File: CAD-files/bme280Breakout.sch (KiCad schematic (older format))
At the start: 9 parts, among them J1 Conn_01x04_Male, U1 BME280

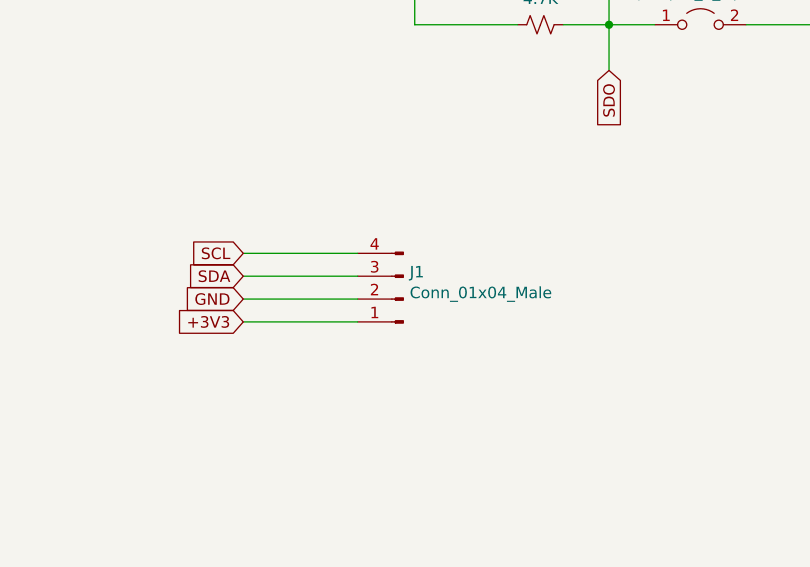
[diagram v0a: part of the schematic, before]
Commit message: added castellated holes
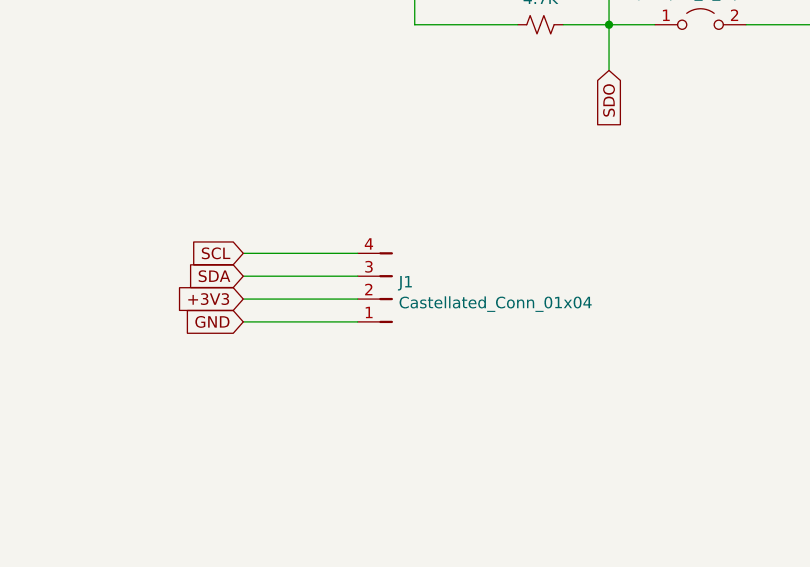
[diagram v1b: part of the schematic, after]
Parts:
- removed J1: Conn_01x04_Male, Connector_PinHeader_2.54mm:PinHeader_1x04_P2.54mm_Vertical, symbol Connector:Conn_01x04_Male
- added J1: Castellated_Conn_01x04, DS-connectors:Castellated_PinHeader_01x04_P2.54mm_Vertical, symbol DS-connectors:Castellated_Conn_01x04
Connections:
- net +3V3: now also J1.2
- net GND: now also J1.1
- net SCL: now also J1.4
- net SDA: now also J1.3
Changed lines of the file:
@@
 Wire Wire Line
 	7600 4550 7600 4350
-$Comp
-L Connector:Conn_01x04_Male J1
-U 1 1 613FE0ED
-P 6700 5550
-F 0 "J1" H 6672 5432 50  0000 R CNN
-F 1 "Conn_01x04_Male" H 6672 5523 50  0000 R CNN
-F 2 "Connector_PinHeader_2.54mm:PinHeader_1x04_P2.54mm_Vertical" H 6700 5550 50  0001 C CNN
-F 3 "~" H 6700 5550 50  0001 C CNN
-	1    6700 5550
-	-1   0    0    1
-$EndComp
 Text GLabel 6000 5350 0    50   Input ~ 0
 SCL
@@
 SDA
 Text GLabel 6000 5550 0    50   Input ~ 0
++3V3
+Text GLabel 6000 5650 0    50   Input ~ 0
 GND
-Text GLabel 6000 5650 0    50   Input ~ 0
-+3V3
 Wire Wire Line
 	6000 5350 6500 5350
@@
 Wire Wire Line
 	2550 5500 2150 5500
+$Comp
+L DS-connectors:Castellated_Conn_01x04 J1
+U 1 1 61534716
+P 6650 5700
+F 0 "J1" H 6620 5476 50  0000 R CNN
+F 1 "Castellated_Conn_01x04" H 6620 5567 50  0000 R CNN
+F 2 "DS-connectors:Castellated_PinHeader_01x04_P2.54mm_Vertical" H 6650 5700 50  0001 C CNN
+F 3 "" H 6650 5700 50  0001 C CNN
+	1    6650 5700
+	-1   0    0    1
+$EndComp
 $EndSCHEMATC

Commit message: Add files via upload
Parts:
- added J2, J3: Castellated_Conn_01x01, DS-connectors:Castellated_PinHeader_01x01_P2.54mm_Vertical, symbol DS-connectors:Castellated_Conn_01x01
- C1, C2: footprint Capacitor_SMD:C_0603_1608Metric -> Capacitor_SMD:C_0805_2012Metric
- R1, R2, R3, R4: footprint Resistor_SMD:R_0603_1608Metric -> Resistor_SMD:R_0805_2012Metric
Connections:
- net GND: now also J2.1, J3.1
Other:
- note removed: "09/14/2021"
- note removed: "2"
- note removed: "BME280 Breakout Board"
- moved on the sheet: C1, C2, J1, JP1, R1, R2, R3, R4, U1
